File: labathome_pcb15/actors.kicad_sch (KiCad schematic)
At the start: 39 parts, among them J18 K1, J24 K1, J7 FAN5V, J8 3V GN RGB 5V, K1 G6K-2, Q1 BC817, Q2 IRLML6344, Q3 TIP41, Q4 BC817, Q5 IRLML6344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

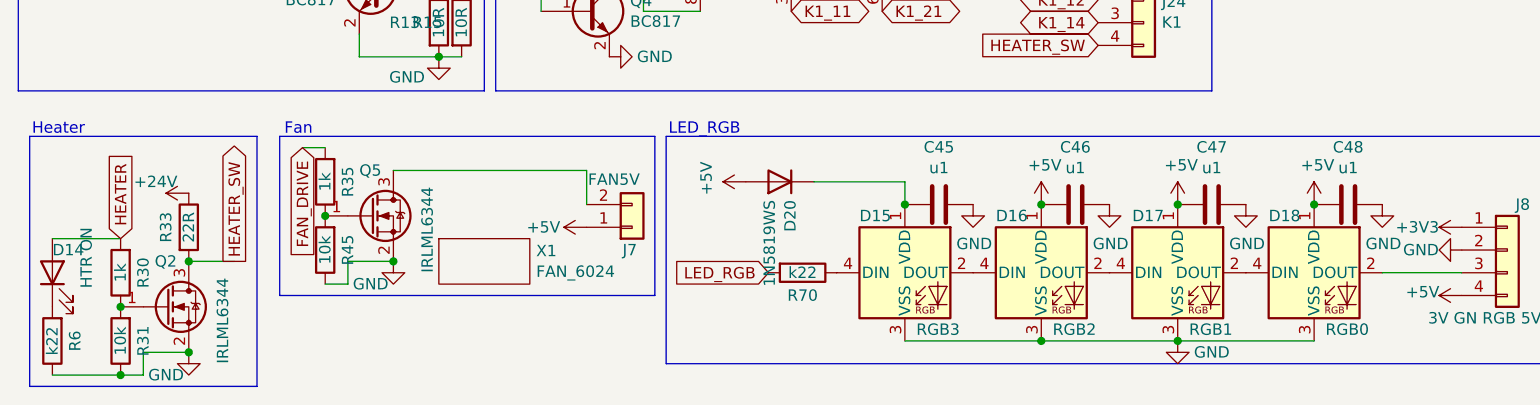
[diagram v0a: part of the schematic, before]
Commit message: Reverse mount LEDs, switch
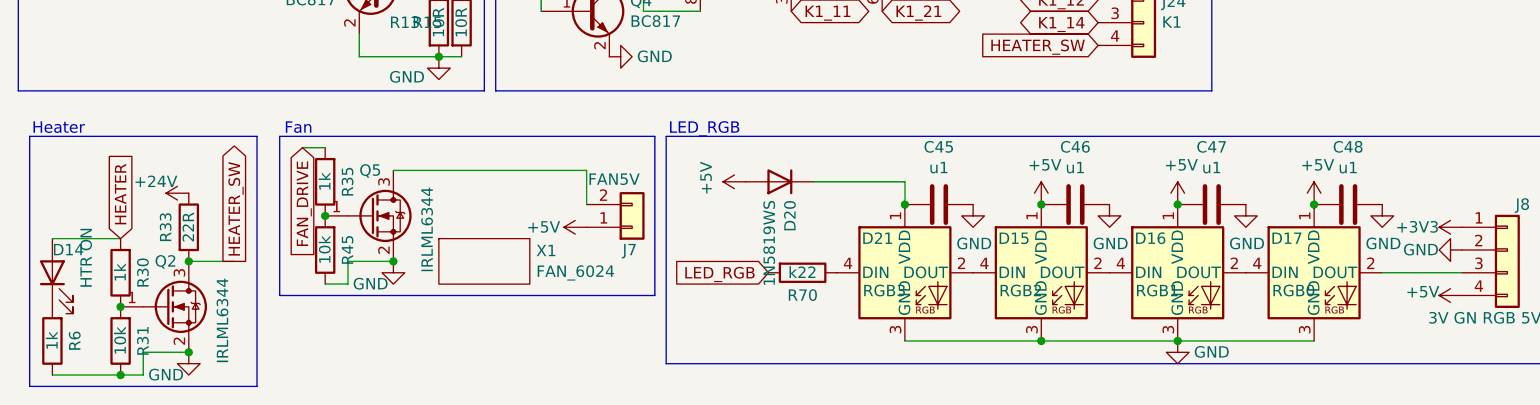
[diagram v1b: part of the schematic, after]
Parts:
- removed D15: RGB3, liebler_OPTO:WS2812b_handsolder, symbol LED:WS2812B
- removed D16: RGB2, liebler_OPTO:WS2812b_handsolder, symbol LED:WS2812B
- removed D17: RGB1, liebler_OPTO:WS2812b_handsolder, symbol LED:WS2812B
- removed D18: RGB0, liebler_OPTO:WS2812b_handsolder, symbol LED:WS2812B
- added D15: RGB2, liebler_OPTO:SK6812MINI-E_REV, symbol liebler_OPTO:SK6812MINI-E_Reverse
- added D16: RGB1, liebler_OPTO:SK6812MINI-E_REV, symbol liebler_OPTO:SK6812MINI-E_Reverse
- added D17: RGB0, liebler_OPTO:SK6812MINI-E_REV, symbol liebler_OPTO:SK6812MINI-E_Reverse
- added D21: RGB3, liebler_OPTO:SK6812MINI-E_REV, symbol liebler_OPTO:SK6812MINI-E_Reverse
- D14: footprint LED_SMD:LED_0805_2012Metric_Pad1.15x1.40mm_HandSolder -> liebler_OPTO:LED_1206_3216Metric_ReverseMount
- R6: value k22 -> 1k
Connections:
- net +5V: now also D15.1 (VDD), D16.1 (VDD), D17.1 (VDD)
- net GND: now also D15.3 (GND), D16.3 (GND), D17.3 (GND), D21.3 (GND)
- net at J8.3 (Pin_3): now also D17.2 (DOUT)
- net at R70.1: now also D21.4 (DIN)
- net at C45.2, D20.1 (K): now also D21.1 (VDD)
- new net: D16.2 (DOUT), D17.4 (DIN)
- new net: D15.2 (DOUT), D16.4 (DIN)
- new net: D15.4 (DIN), D21.2 (DOUT)

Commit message: Various last minute
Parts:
- C45, C46, C47, C48: footprint Capacitor_SMD:C_0402_1005Metric -> Capacitor_SMD:C_0201_0603Metric
- R31, R45: footprint Resistor_SMD:R_0402_1005Metric -> Resistor_SMD:R_0201_0603Metric
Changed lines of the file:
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@@
 			)
 		)
-		(property "Footprint" "Resistor_SMD:R_0402_1005Metric"
+		(property "Footprint" "Resistor_SMD:R_0201_0603Metric"
 			(at 27.178 77.47 90)
 			(effects
@@
 			)
 		)
-		(property "Footprint" "Capacitor_SMD:C_0402_1005Metric"
+		(property "Footprint" "Capacitor_SMD:C_0201_0603Metric"
 			(at 158.75 63.1952 0)
 			(effects
@@
 			)
 		)
-		(property "Footprint" "Resistor_SMD:R_0402_1005Metric"
+		(property "Footprint" "Resistor_SMD:R_0201_0603Metric"
 			(at 50.038 67.31 90)
 			(effects
@@
 			)
 		)
-		(property "Footprint" "Capacitor_SMD:C_0402_1005Metric"
+		(property "Footprint" "Capacitor_SMD:C_0201_0603Metric"
 			(at 113.03 63.1952 0)
 			(effects
@@
 			)
 		)
-		(property "Footprint" "Capacitor_SMD:C_0402_1005Metric"
+		(property "Footprint" "Capacitor_SMD:C_0201_0603Metric"
 			(at 128.27 63.1952 0)
 			(effects
@@
 			)
 		)
-		(property "Footprint" "Capacitor_SMD:C_0402_1005Metric"
+		(property "Footprint" "Capacitor_SMD:C_0201_0603Metric"
 			(at 143.51 63.1952 0)
 			(effects

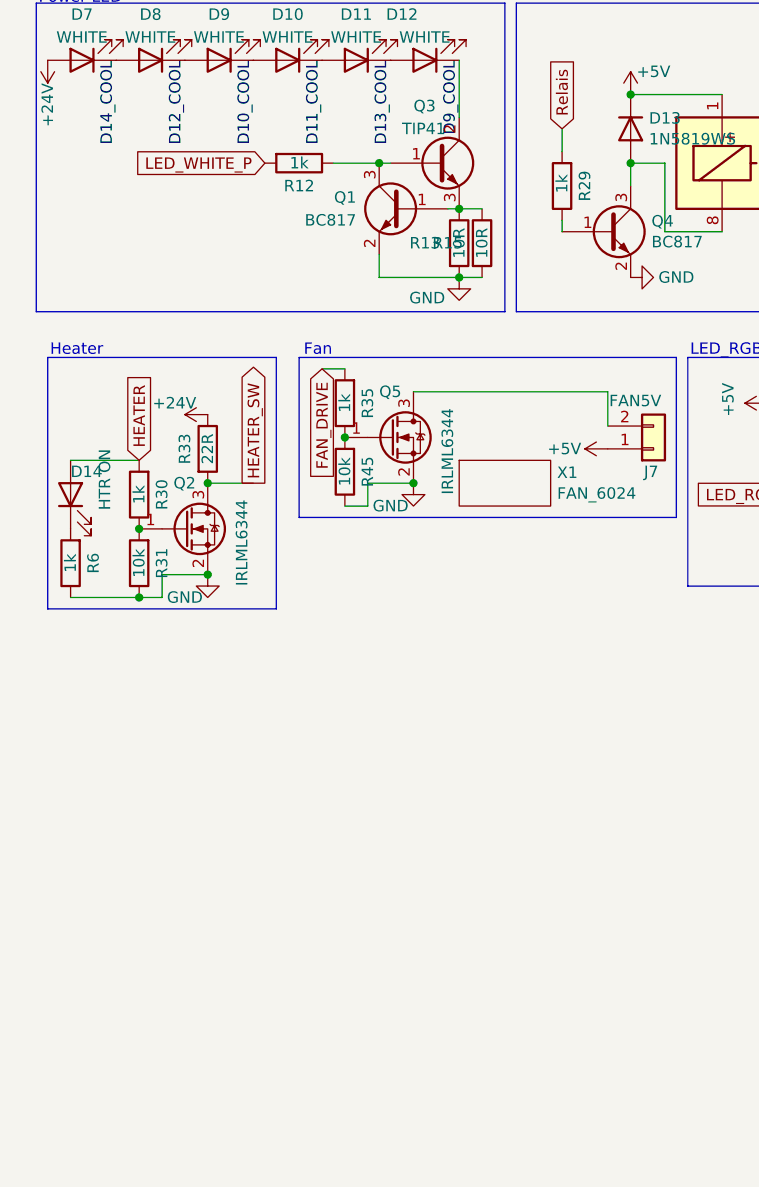
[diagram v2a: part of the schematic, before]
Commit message: ec11 smd, LCD Reset from ESP32 with jumper, six servos
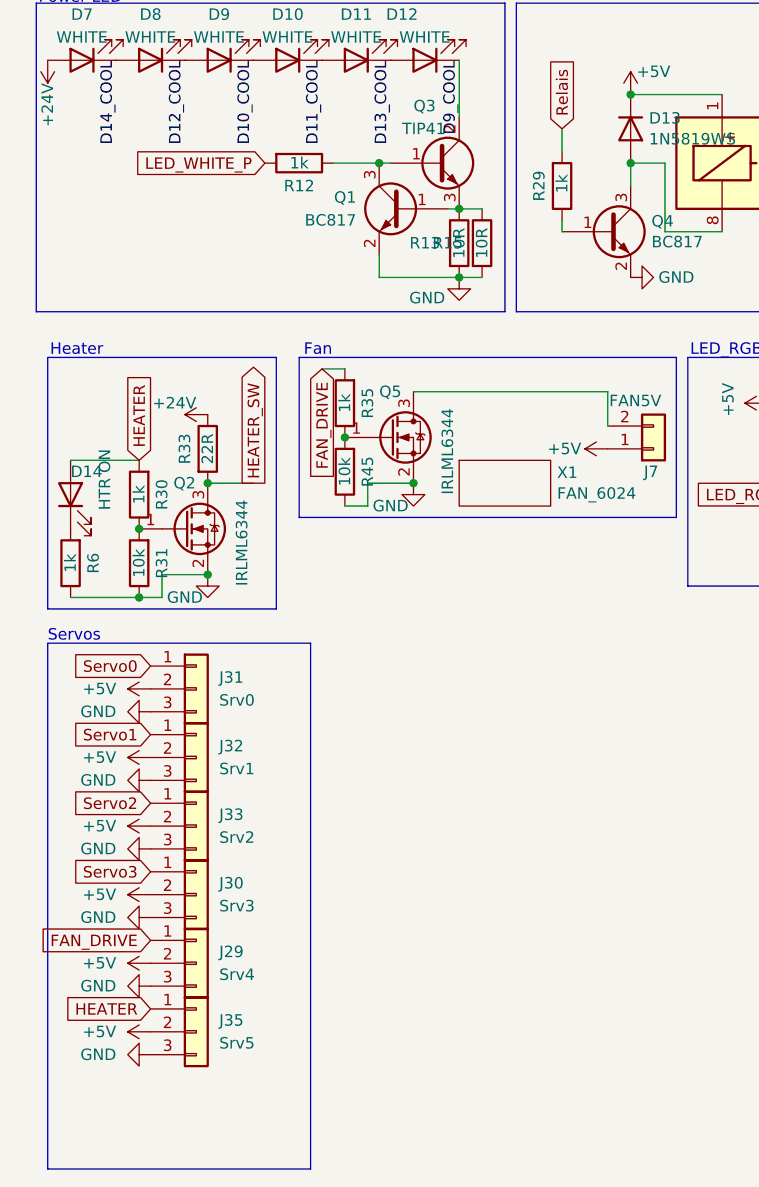
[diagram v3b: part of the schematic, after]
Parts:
- added J29: Srv4, liebler_CONN:PinHeader_1x03_P2.54mm_Vertical_smallerCourtyard, symbol Connector_Generic:Conn_01x03
- added J30: Srv3, liebler_CONN:PinHeader_1x03_P2.54mm_Vertical_smallerCourtyard, symbol Connector_Generic:Conn_01x03
- added J31: Srv0, liebler_CONN:PinHeader_1x03_P2.54mm_Vertical_smallerCourtyard, symbol Connector_Generic:Conn_01x03
- added J32: Srv1, liebler_CONN:PinHeader_1x03_P2.54mm_Vertical_smallerCourtyard, symbol Connector_Generic:Conn_01x03
- added J33: Srv2, liebler_CONN:PinHeader_1x03_P2.54mm_Vertical_smallerCourtyard, symbol Connector_Generic:Conn_01x03
- added J35: Srv5, liebler_CONN:PinHeader_1x03_P2.54mm_Vertical_smallerCourtyard, symbol Connector_Generic:Conn_01x03
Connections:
- net +5V: now also J29.2 (Pin_2), J30.2 (Pin_2), J31.2 (Pin_2), J32.2 (Pin_2), J33.2 (Pin_2), J35.2 (Pin_2)
- net FAN_DRIVE: now also J29.1 (Pin_1)
- net GND: now also J29.3 (Pin_3), J30.3 (Pin_3), J31.3 (Pin_3), J32.3 (Pin_3), J33.3 (Pin_3), J35.3 (Pin_3)
- net HEATER: now also J35.1 (Pin_1)
- new net Servo0: J31.1 (Pin_1)
- new net Servo1: J32.1 (Pin_1)
- new net Servo2: J33.1 (Pin_1)
- new net Servo3: J30.1 (Pin_1)
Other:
- note added: "Servos"
- moved on the sheet: R29

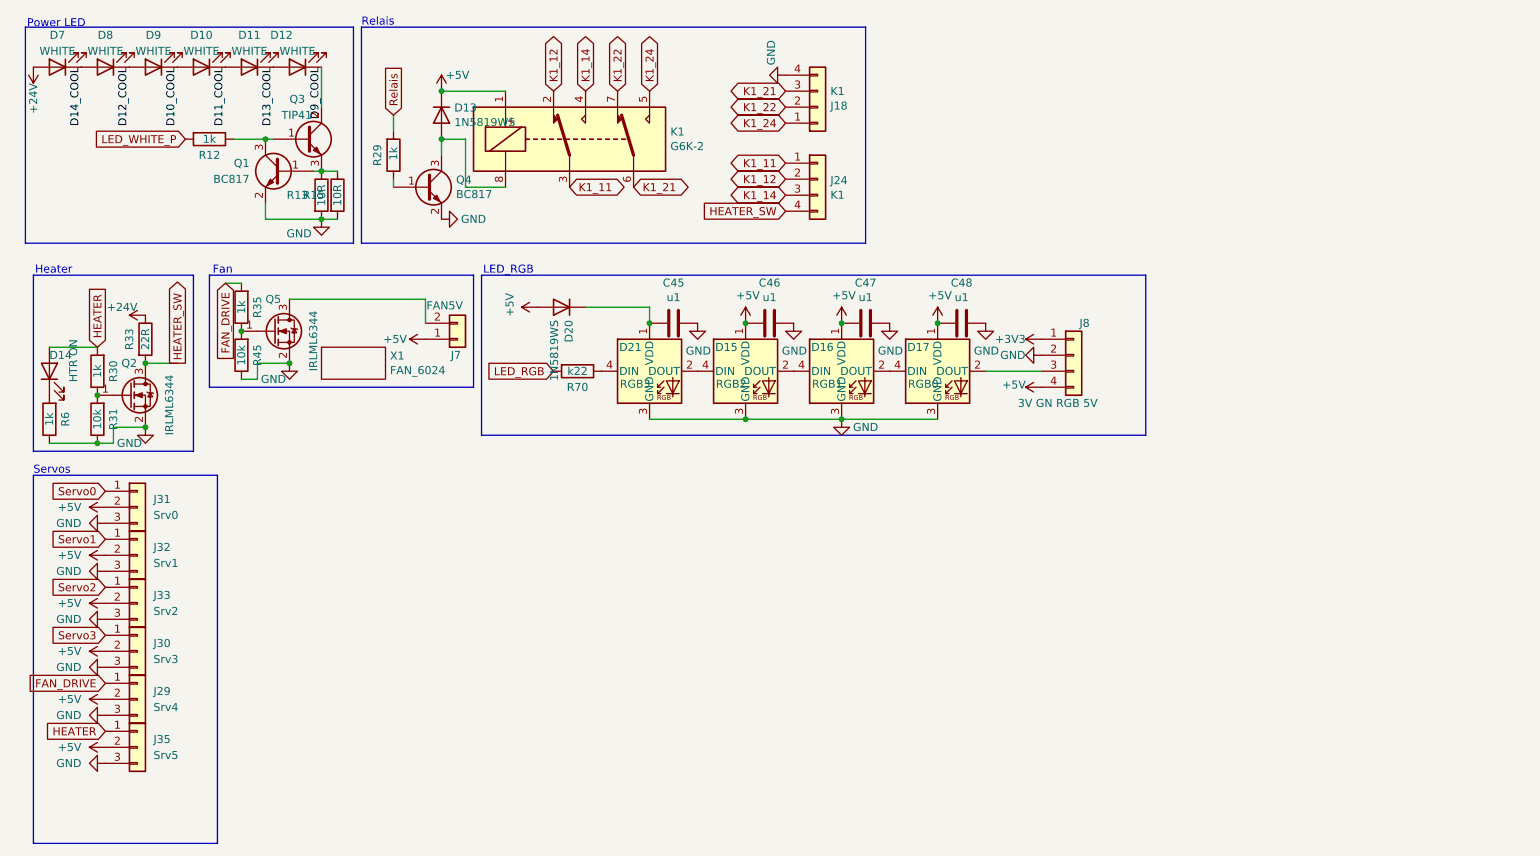
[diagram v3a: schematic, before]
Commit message: Updated PCB, sensprs as JSON
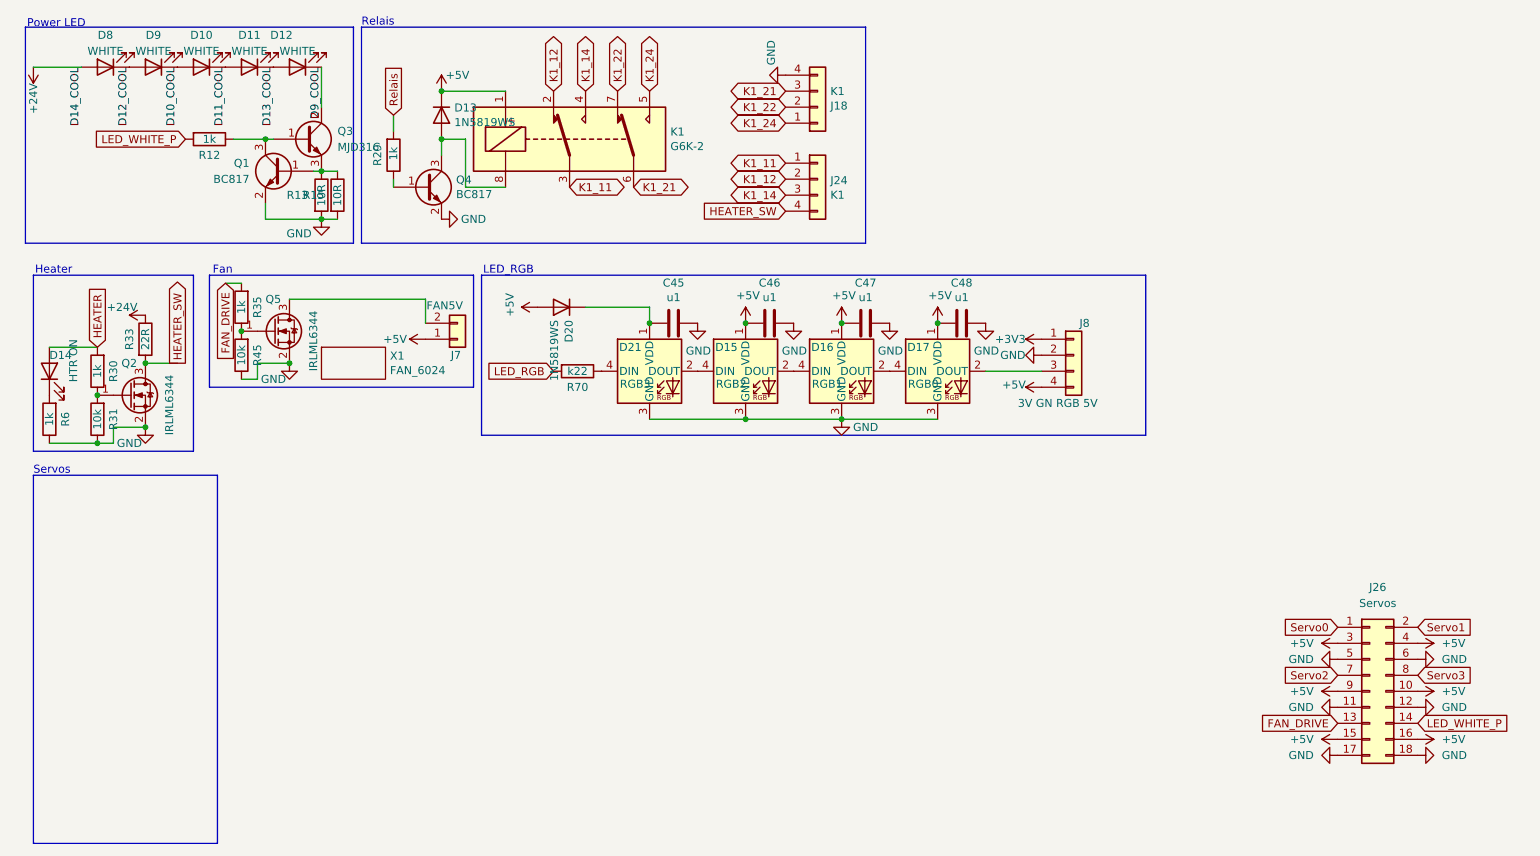
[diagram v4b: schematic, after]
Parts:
- removed D7: WHITE, liebler_OPTO:LED_PLCC_2835_Handsoldering, symbol Device:LED
- removed J29: Srv4, liebler_CONN:PinHeader_1x03_P2.54mm_Vertical_smallerCourtyard, symbol Connector_Generic:Conn_01x03
- removed J30: Srv3, liebler_CONN:PinHeader_1x03_P2.54mm_Vertical_smallerCourtyard, symbol Connector_Generic:Conn_01x03
- removed J31: Srv0, liebler_CONN:PinHeader_1x03_P2.54mm_Vertical_smallerCourtyard, symbol Connector_Generic:Conn_01x03
- removed J32: Srv1, liebler_CONN:PinHeader_1x03_P2.54mm_Vertical_smallerCourtyard, symbol Connector_Generic:Conn_01x03
- removed J33: Srv2, liebler_CONN:PinHeader_1x03_P2.54mm_Vertical_smallerCourtyard, symbol Connector_Generic:Conn_01x03
- removed J35: Srv5, liebler_CONN:PinHeader_1x03_P2.54mm_Vertical_smallerCourtyard, symbol Connector_Generic:Conn_01x03
- removed Q3: TIP41, Package_TO_SOT_THT:TO-220-3_Horizontal_TabUp, symbol Transistor_BJT:TIP41
- added J26: Servos, Connector_PinHeader_2.54mm:PinHeader_2x09_P2.54mm_Horizontal, symbol Connector_Generic:Conn_02x09_Odd_Even
- added Q3: MJD31C, Package_TO_SOT_SMD:TO-252-2, symbol Device:Q_NPN_BCE
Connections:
- net D14_COOL is gone; now on net +24V: D8.2 (A)
- net +5V: now also J26.10 (Pin_10), J26.15 (Pin_15), J26.16 (Pin_16), J26.3 (Pin_3), J26.4 (Pin_4), J26.9 (Pin_9)
- net D9_COOL: now also Q3.2 (C)
- net FAN_DRIVE: now also J26.13 (Pin_13)
- net GND: now also J26.11 (Pin_11), J26.12 (Pin_12), J26.17 (Pin_17), J26.18 (Pin_18), J26.5 (Pin_5), J26.6 (Pin_6)
- net LED_WHITE_P: now also J26.14 (Pin_14)
- net Servo0: now also J26.1 (Pin_1)
- net Servo1: now also J26.2 (Pin_2)
- net Servo2: now also J26.7 (Pin_7)
- net Servo3: now also J26.8 (Pin_8)
- net at Q1.3 (C), R12.1: now also Q3.1 (B)
- net at Q1.1 (B), R13.1, R15.1: now also Q3.3 (E)

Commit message: IP5306
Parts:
- J26: footprint Connector_PinHeader_2.54mm:PinHeader_2x09_P2.54mm_Horizontal -> liebler_CONN:PinHeader_2x09_P2.54mm_Horizontal_SMD
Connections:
- net FAN_DRIVE: now also J26.5 (Pin_5); no longer J26.13 (Pin_13)
- net GND: now also J26.1 (Pin_1), J26.13 (Pin_13), J26.14 (Pin_14), J26.2 (Pin_2), J26.7 (Pin_7), J26.8 (Pin_8); no longer J26.11 (Pin_11), J26.12 (Pin_12), J26.17 (Pin_17), J26.18 (Pin_18), J26.5 (Pin_5), J26.6 (Pin_6)
- net LED_WHITE_P: now also J26.6 (Pin_6); no longer J26.14 (Pin_14)
- net Servo0: now also J26.17 (Pin_17); no longer J26.1 (Pin_1)
- net Servo1: now also J26.18 (Pin_18); no longer J26.2 (Pin_2)
- net Servo2: now also J26.11 (Pin_11); no longer J26.7 (Pin_7)
- net Servo3: now also J26.12 (Pin_12); no longer J26.8 (Pin_8)
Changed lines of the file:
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@@
 		(lib_id "Connector_Generic:Conn_02x09_Odd_Even")
 		(at 227.33 120.65 0)
+		(mirror x)
 		(unit 1)
 		(exclude_from_sim no)
@@
 		(on_board yes)
 		(dnp no)
-		(fields_autoplaced yes)
 		(property "Reference" "J26"
-			(at 228.6 104.14 0)
+			(at 228.6 137.16 0)
 			(effects
 				(font
@@
 		)
 		(property "Value" "Servos"
-			(at 228.6 106.68 0)
+			(at 228.6 134.62 0)
 			(effects
 				(font
@@
 			)
 		)
-		(property "Footprint" "Connector_PinHeader_2.54mm:PinHeader_2x09_P2.54mm_Horizontal"
+		(property "Footprint" "liebler_CONN:PinHeader_2x09_P2.54mm_Horizontal_SMD"
 			(at 227.33 120.65 0)
 			(effects
